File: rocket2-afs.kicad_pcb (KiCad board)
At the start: 4 copper layers, 70 x 50 mm, 72 parts, among them J1 ARMING_PLUG, J2 POWER, J3 E-MATCH_DROGUE, J4 SWD, J5 E-MATCH_RECOVERY, Q1 Q_NMOS_GSD, Q2 Q_NMOS_GSD, Q3 Q_NMOS_GSD, Q4 Q_NMOS_GSD, Q5 Q_NMOS_GSD, U2 LD1086DT33TR, U8 USBLC6-2SC6, Y1 16MHz

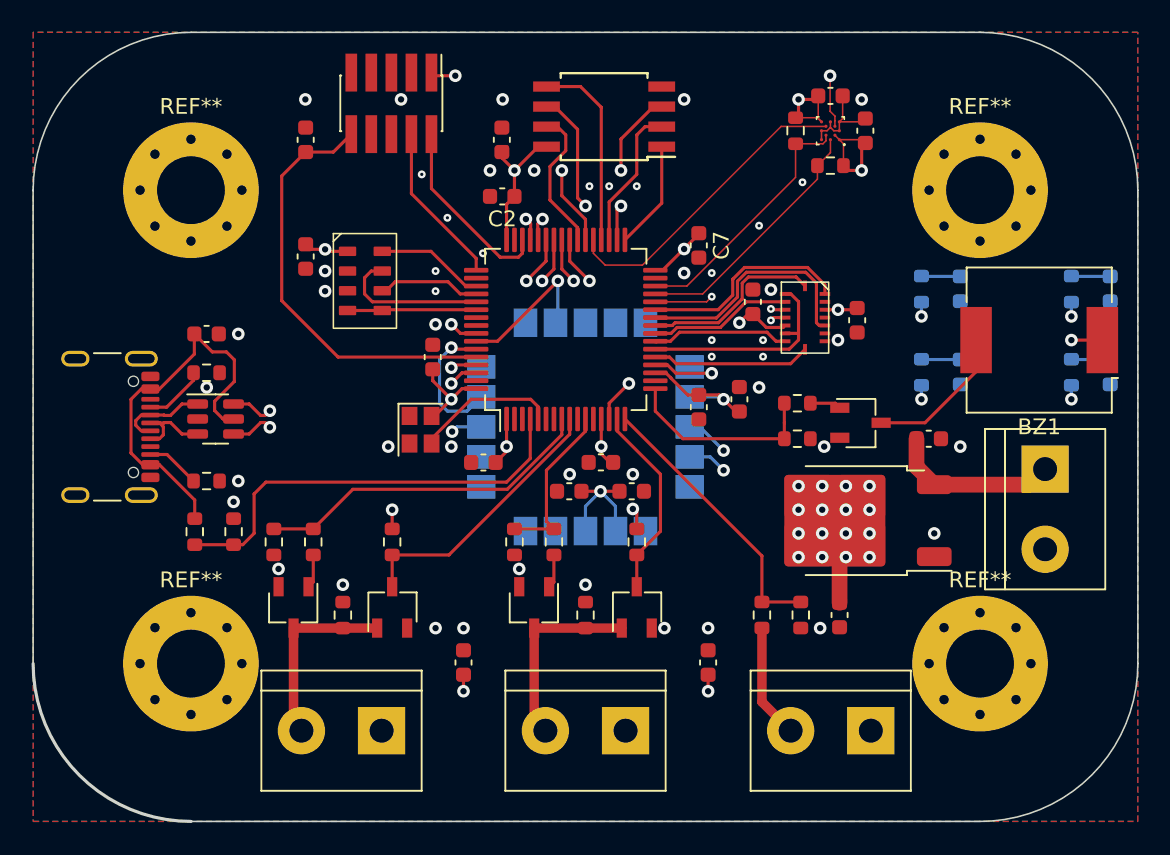
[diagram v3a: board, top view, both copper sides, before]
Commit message: Moved All Thick Components to "Front" Layer. Added Silkscreens
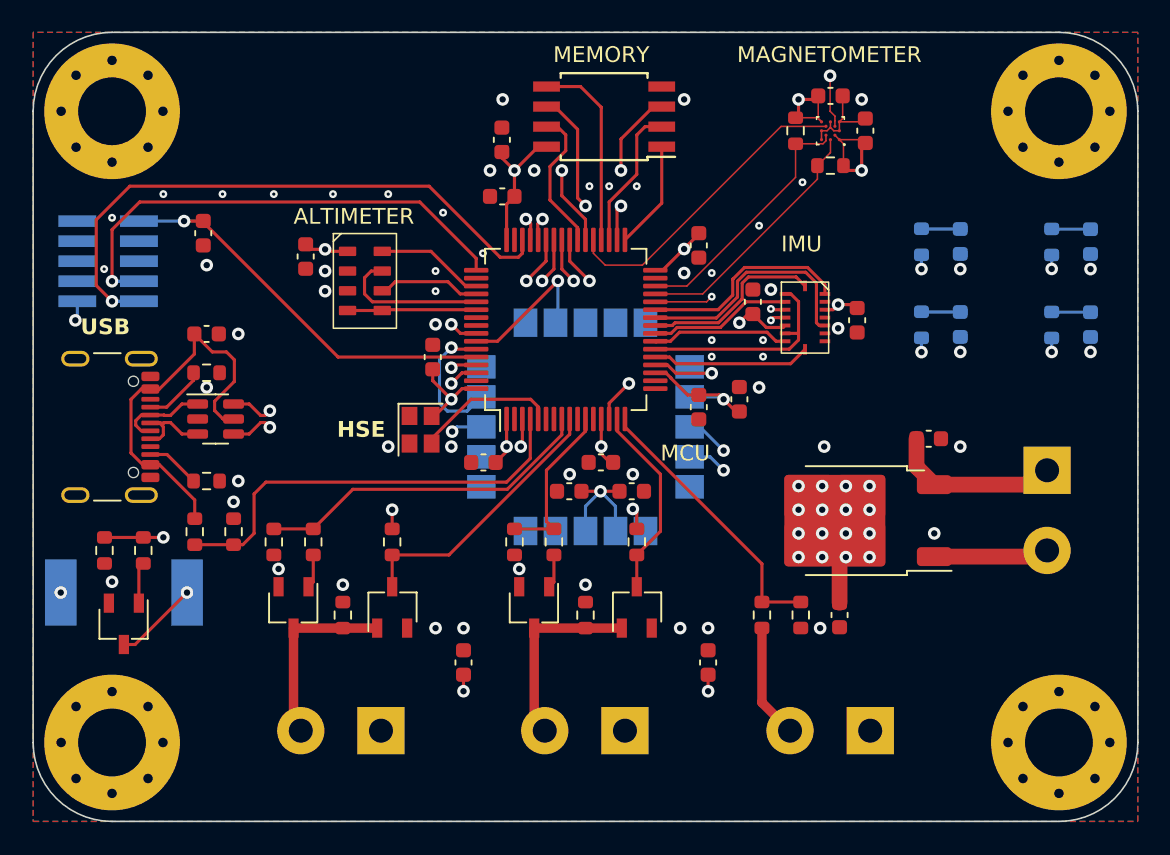
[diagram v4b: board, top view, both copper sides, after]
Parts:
- BZ1, J1, J2, J3, J4, J5: moved to B.Cu
- moved BZ1 60.2 mm to (125.8, 95.5), turned to 0 degrees
- moved Q5 48.4 mm to (125.8, 97.5), turned to -90 degrees
- moved R19 44.5 mm to (124.5, 92.8), turned to -90 degrees
- moved R20 42.5 mm to (127.0, 92.8), turned to -90 degrees
- moved J4 20.5 mm to (124.8, 74.5), turned to 0 degrees
- moved R9 11.7 mm to (184.5, 73.3)
- moved D3 11.7 mm to (187.0, 73.3)
- moved D2 9.77 mm to (178.8, 78.5)
- moved R7 9.77 mm to (176.3, 78.5)
- moved C1 8.78 mm to (130.8, 72.7), turned to 90 degrees
- moved REF** 7.07 mm to (125.0, 105.0)
- moved REF** 7.07 mm to (125.0, 65.0)
- moved REF** 7.07 mm to (185.0, 105.0)
- moved REF** 7.07 mm to (185.0, 65.0)
- moved D4 3.25 mm to (187.0, 78.5)
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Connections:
- U1 pad 17: BUZZER -> unconnected-(U1-PA3-Pad17)
- U1 pad 3: unconnected-(U1-PC14-Pad3) -> BUZZER
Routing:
- net DEBUG_SWDIO: track 12.0 -> 38.0 mm, vias 0 -> 1
- net DEBUCK_SWCLK: track 10.3 -> 31.0 mm, vias 0 -> 1
- net BUZZER: track 12.6 -> 30.6 mm, vias 0 -> 2
- net LED_STANDBY: track 34.6 -> 48.8 mm
- net LED_FLIGHT: track 44.6 -> 35.4 mm
- net GND: track 6.25 -> 13.6 mm, vias 49 -> 59
- net Net-(BZ1--): track 9.36 -> 5.36 mm, vias 0 -> 1
- net LED_ARMED: track 36.2 -> 39.2 mm
- net +3.3V: track 74.7 -> 72.6 mm
- net NRST: track 27.2 -> 26.2 mm, vias 0 -> 1
- net Net-(Q5-G): track 1.99 -> 2.63 mm
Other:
- outline, holes or cut-outs redrawn
- board text added: "(+)"
- board text added: "ALTIMETER"
- board text added: "ARMED"
- board text added: "ARMING PLUG"
- board text added: "BUZZER"
- board text added: "Caden Nguyen Robert Woo Eesh Vij Daniel He"
- board text added: "DEBUG"
- board text added: "DROGUE"
- board text added: "FLIGHT"
- board text added: "GPS"
- board text added: "HSE"
- board text added: "IMU"
- board text added: "MAGNETOMETER"
- board text added: "MAIN"
- board text added: "MCU"
- board text added: "MEMORY"
- board text added: "POWER"
- board text added: "STANDBY"
- board text added: "STORAGE"
- board text added: "UCI Rocket Project - Avionics Avionics Flight System Betelgeuse v2.1 03/12/2024"
- board text added: "USB"

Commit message: Silkscreen update.
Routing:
- net +3.3V: track 72.6 -> 73.2 mm
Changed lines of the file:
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@@
     )
     (stroke (width 0) (type solid)) (fill solid) (layer "B.SilkS"))
-  (gr_rect (start 160 65.25) (end 168.5 70.75)
+  (gr_rect (start 132.6875 62.25) (end 141.1875 67.75)
     (stroke (width 0.15) (type dash)) (fill none) (layer "B.SilkS"))
   (gr_poly
@@
     (effects (font (size 1 1) (thickness 0.1875) bold) (justify left bottom mirror))
   )
-  (gr_text "DEBUG" (at 134.25 69) (layer "B.SilkS")
+  (gr_text "DEBUG" (at 127.407441 79.75) (layer "B.SilkS")
     (effects (font (size 1 1) (thickness 0.1875) bold) (justify left bottom mirror))
   )
@@
     (effects (font (size 1 1) (thickness 0.1875) bold) (justify left bottom mirror))
   )
-  (gr_text "Caden Nguyen\nRobert Woo\nEesh Vij\nDaniel He" (at 164.25 70.25) (layer "B.SilkS")
+  (gr_text "Caden Nguyen\nRobert Woo\nEesh Vij\nDaniel He" (at 136.9375 67.30925) (layer "B.SilkS")
     (effects (font (size 0.75 0.75) (thickness 0.15)) (justify bottom mirror))
   )
@@
   (via (at 170 90.25) (size 0.8) (drill 0.4) (layers "F.Cu" "B.Cu") (net 3))
   (via (at 138.5 73.75) (size 0.8) (drill 0.4) (layers "F.Cu" "B.Cu") (net 3))
-  (via (at 122.675 78.25) (size 0.8) (drill 0.4) (layers "F.Cu" "B.Cu") (net 3))
+  (via (at 121.5 78.25) (size 0.8) (drill 0.4) (layers "F.Cu" "B.Cu") (net 3))
   (via (at 168.5 91.75) (size 0.8) (drill 0.4) (layers "F.Cu" "B.Cu") (net 3))
   (via (at 150.5 68.75) (size 0.8) (drill 0.4) (layers "F.Cu" "B.Cu") (net 3))
@@
   (segment (start 155.95 89.08) (end 156.9 90.03) (width 0.2) (layer "B.Cu") (net 3))
   (segment (start 163.75 83.25) (end 163.6 83.1) (width 0.2) (layer "B.Cu") (net 3))
-  (segment (start 122.8 77.04) (end 122.8 78.125) (width 0.2) (layer "B.Cu") (net 3))
-  (segment (start 122.8 78.125) (end 122.675 78.25) (width 0.2) (layer "B.Cu") (net 3))
+  (segment (start 121.59 78.25) (end 122.8 77.04) (width 0.2) (layer "B.Cu") (net 3))
   (segment (start 155.95 89.08) (end 155 90.03) (width 0.2) (layer "B.Cu") (net 3))
   (segment (start 163.6 83.1) (end 161.6 83.1) (width 0.2) (layer "B.Cu") (net 3))
+  (segment (start 121.5 78.25) (end 121.59 78.25) (width 0.2) (layer "B.Cu") (net 3))
   (segment (start 156.9 90.03) (end 156.9 91.6) (width 0.2) (layer "B.Cu") (net 3))
   (segment (start 166.18 97.745) (end 166.18 102.47) (width 0.6) (layer "F.Cu") (net 4))

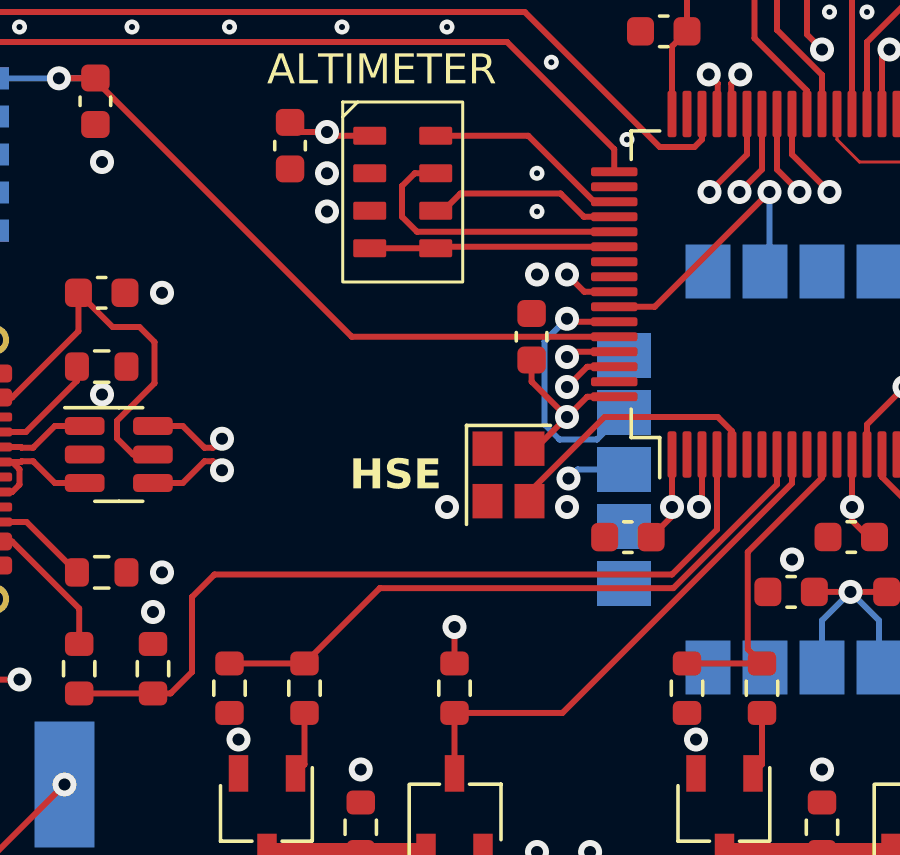
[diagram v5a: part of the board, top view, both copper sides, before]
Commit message: Adjusted VBUS
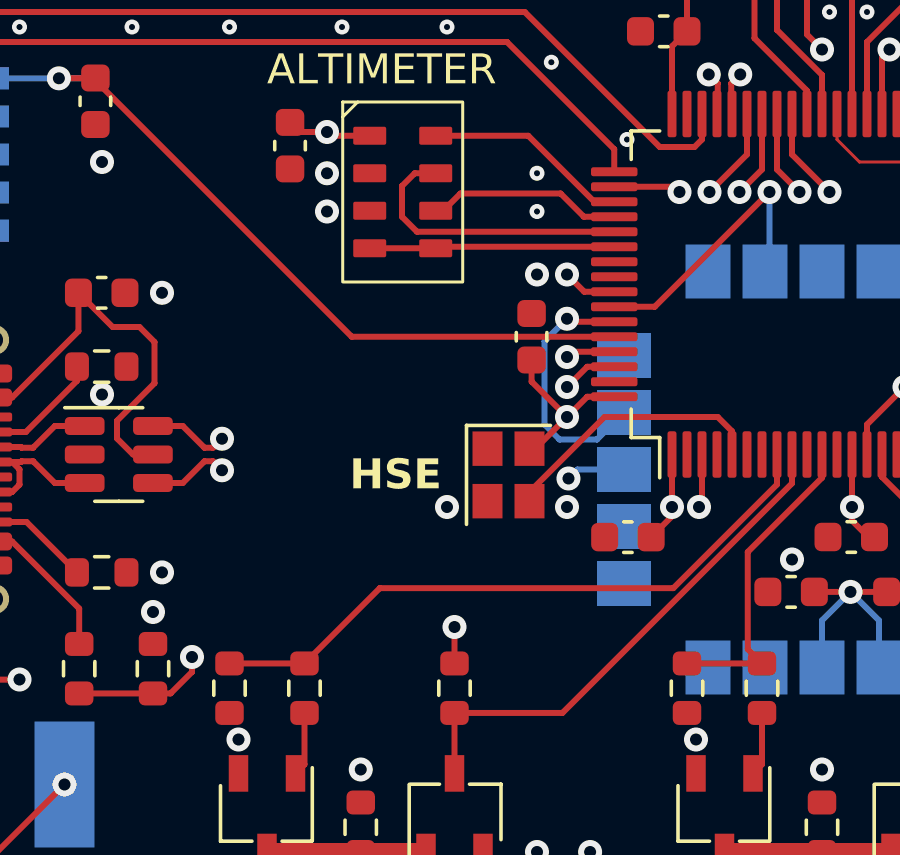
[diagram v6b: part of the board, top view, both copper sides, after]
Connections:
- U1 pad 4: VBUS_SENS -> unconnected-(U1-PC15-Pad4)
- U1 pad 42: LED_STANDBY -> VBUS_SENS
- U1 pad 43: LED_STORAGE -> LED_STANDBY
- U1 pad 50: unconnected-(U1-PA15-Pad50) -> LED_STORAGE
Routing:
- net VBUS_SENS: track 27.5 -> 40.0 mm, vias 0 -> 2
- net LED_STANDBY: track 48.8 -> 49.4 mm
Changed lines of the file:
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@@
   (net 41 "ALT_MOSI")
   (net 42 "ALT_CS")
-  (net 43 "unconnected-(U1-PA15-Pad50)")
+  (net 43 "unconnected-(U1-PC15-Pad4)")
   (net 44 "MAG_DRDY")
   (net 45 "MAG_INT")
@@
       (net 75 "BUZZER") (pinfunction "PC14") (pintype "bidirectional"))
     (pad "4" smd roundrect (at -5.675 -2.25 90) (size 1.55 0.3) (layers "F.Cu" "F.Paste" "F.Mask") (roundrect_rratio 0.25)
-      (net 77 "VBUS_SENS") (pinfunction "PC15") (pintype "bidirectional"))
+      (net 43 "unconnected-(U1-PC15-Pad4)") (pinfunction "PC15") (pintype "bidirectional+no_connect"))
     (pad "5" smd roundrect (at -5.675 -1.75 90) (size 1.55 0.3) (layers "F.Cu" "F.Paste" "F.Mask") (roundrect_rratio 0.25)
       (net 37 "HSE_IN") (pinfunction "PD0") (pintype "bidirectional"))
@@
       (net 30 "LED_FLIGHT") (pinfunction "PA8") (pintype "bidirectional"))
     (pad "42" smd roundrect (at 5.675 -0.75 90) (size 1.55 0.3) (layers "F.Cu" "F.Paste" "F.Mask") (roundrect_rratio 0.25)
-      (net 31 "LED_STANDBY") (pinfunction "PA9") (pintype "bidirectional"))
+      (net 77 "VBUS_SENS") (pinfunction "PA9") (pintype "bidirectional"))
     (pad "43" smd roundrect (at 5.675 -1.25 90) (size 1.55 0.3) (layers "F.Cu" "F.Paste" "F.Mask") (roundrect_rratio 0.25)
-      (net 32 "LED_STORAGE") (pinfunction "PA10") (pintype "bidirectional"))
+      (net 31 "LED_STANDBY") (pinfunction "PA10") (pintype "bidirectional"))
     (pad "44" smd roundrect (at 5.675 -1.75 90) (size 1.55 0.3) (layers "F.Cu" "F.Paste" "F.Mask") (roundrect_rratio 0.25)
       (net 70 "USB_D-") (pinfunction "PA11") (pintype "bidirectional"))
@@
       (net 12 "DEBUCK_SWCLK") (pinfunction "PA14") (pintype "bidirectional"))
     (pad "50" smd roundrect (at 3.25 -5.675 90) (size 0.3 1.55) (layers "F.Cu" "F.Paste" "F.Mask") (roundrect_rratio 0.25)
-      (net 43 "unconnected-(U1-PA15-Pad50)") (pinfunction "PA15") (pintype "bidirectional+no_connect"))
+      (net 32 "LED_STORAGE") (pinfunction "PA15") (pintype "bidirectional"))
     (pad "51" smd roundrect (at 2.75 -5.675 90) (size 0.3 1.55) (layers "F.Cu" "F.Paste" "F.Mask") (roundrect_rratio 0.25)
       (net 39 "ALT_SCK") (pinfunction "PC10") (pintype "bidirectional"))
@@
   (segment (start 154.25 75.75) (end 154.25 80.75) (width 0.2) (layer "In1.Cu") (net 30))
   (segment (start 176.29 79.365) (end 176.29 80.25) (width 0.2) (layer "B.Cu") (net 30))
-  (segment (start 153 75) (end 153 73.15) (width 0.2) (layer "F.Cu") (net 31))
-  (segment (start 152.25 75.75) (end 153 75) (width 0.2) (layer "F.Cu") (net 31))
+  (segment (start 152.5 74.5) (end 152.5 73.15) (width 0.2) (layer "F.Cu") (net 31))
+  (segment (start 151.25 75.75) (end 152.5 74.5) (width 0.2) (layer "F.Cu") (net 31))
   (via (at 184.54 74.99) (size 0.8) (drill 0.4) (layers "F.Cu" "B.Cu") (net 31))
-  (via (at 152.25 75.75) (size 0.8) (drill 0.4) (layers "F.Cu" "B.Cu") (net 31))
-  (segment (start 182.875 81) (end 178.5 81) (width 0.2) (layer "In1.Cu") (net 31))
+  (via (at 151.25 75.75) (size 0.8) (drill 0.4) (layers "F.Cu" "B.Cu") (net 31))
+  (segment (start 183.5 80.375) (end 182.875 81) (width 0.2) (layer "In1.Cu") (net 31))
   (segment (start 184.54 74.99) (end 183.5 76.03) (width 0.2) (layer "In1.Cu") (net 31))
+  (segment (start 151.25 78.5) (end 151.25 75.75) (width 0.2) (layer "In1.Cu") (net 31))
+  (segment (start 157.75 85) (end 151.25 78.5) (width 0.2) (layer "In1.Cu") (net 31))
+  (segment (start 182.875 81) (end 178.5 81) (width 0.2) (layer "In1.Cu") (net 31))
   (segment (start 183.5 76.03) (end 183.5 80.375) (width 0.2) (layer "In1.Cu") (net 31))
-  (segment (start 183.5 80.375) (end 182.875 81) (width 0.2) (layer "In1.Cu") (net 31))
   (segment (start 174.5 85) (end 157.75 85) (width 0.2) (layer "In1.Cu") (net 31))
   (segment (start 178.5 81) (end 174.5 85) (width 0.2) (layer "In1.Cu") (net 31))
-  (segment (start 157.75 85) (end 152.25 79.5) (width 0.2) (layer "In1.Cu") (net 31))
-  (segment (start 152.25 79.5) (end 152.25 75.75) (width 0.2) (layer "In1.Cu") (net 31))
   (segment (start 184.54 74.105) (end 184.54 74.99) (width 0.2) (layer "B.Cu") (net 31))
-  (segment (start 152.5 74.5) (end 152.5 73.15) (width 0.2) (layer "F.Cu") (net 32))
-  (segment (start 151.25 75.75) (end 152.5 74.5) (width 0.2) (layer "F.Cu") (net 32))
-  (via (at 151.25 75.75) (size 0.8) (drill 0.4) (layers "F.Cu" "B.Cu") (net 32))
+  (segment (start 150.075 75.575) (end 150.25 75.75) (width 0.2) (layer "F.Cu") (net 32))
+  (segment (start 148.075 75.575) (end 150.075 75.575) (width 0.2) (layer "F.Cu") (net 32))
+  (via (at 150.25 75.75) (size 0.8) (drill 0.4) (layers "F.Cu" "B.Cu") (net 32))
   (via (at 184.54 80.25) (size 0.8) (drill 0.4) (layers "F.Cu" "B.Cu") (free) (net 32))
-  (segment (start 151.25 79.25) (end 157.5 85.5) (width 0.2) (layer "In1.Cu") (net 32))
-  (segment (start 184.54 80.25) (end 183.29 81.5) (width 0.2) (layer "In1.Cu") (net 32))
-  (segment (start 157.5 85.5) (end 174.75 85.5) (width 0.2) (layer "In1.Cu") (net 32))
-  (segment (start 178.75 81.5) (end 182.5 81.5) (width 0.2) (layer "In1.Cu") (net 32))
-  (segment (start 183.29 81.5) (end 182.5 81.5) (width 0.2) (layer "In1.Cu") (net 32))
-  (segment (start 151.25 75.75) (end 151.25 79.25) (width 0.2) (layer "In1.Cu") (net 32))
+  (segment (start 150.25 78.25) (end 157.5 85.5) (width 0.2) (layer "In1.Cu") (net 32))
+  (segment (start 178.75 81.5) (end 183.29 81.5) (width 0.2) (layer "In1.Cu") (net 32))
   (segment (start 174.75 85.5) (end 178.75 81.5) (width 0.2) (layer "In1.Cu") (net 32))
+  (segment (start 157.5 85.5) (end 174.75 85.5) (width 0.2) (layer "In1.Cu") (net 32))
+  (segment (start 150.25 75.75) (end 150.25 78.25) (width 0.2) (layer "In1.Cu") (net 32))
+  (segment (start 183.29 81.5) (end 184.54 80.25) (width 0.2) (layer "In1.Cu") (net 32))
   (segment (start 184.54 79.365) (end 184.54 80.25) (width 0.2) (layer "B.Cu") (net 32))
   (segment (start 153.25 75.75) (end 149.425 79.575) (width 0.2) (layer "F.Cu") (net 33))
@@
   (segment (start 145.2 92) (end 128.25 92) (width 0.2) (layer "In1.Cu") (net 75))
   (segment (start 150.9 86.25) (end 150.9 86.3) (width 0.2) (layer "In1.Cu") (net 75))
-  (segment (start 151.5 87) (end 151.5 84.5) (width 0.2) (layer "F.Cu") (net 77))
   (segment (start 132.7 92.465) (end 130.24 92.465) (width 0.2) (layer "F.Cu") (net 77))
-  (segment (start 134 91.75) (end 134 89.25) (width 0.2) (layer "F.Cu") (net 77))
-  (segment (start 134 89.25) (end 134.75 88.5) (width 0.2) (layer "F.Cu") (net 77))
-  (segment (start 134.75 88.5) (end 150 88.5) (width 0.2) (layer "F.Cu") (net 77))
+  (segment (start 134 91.75) (end 134 91.25) (width 0.2) (layer "F.Cu") (net 77))
+  (segment (start 153 75) (end 153 73.15) (width 0.2) (layer "F.Cu") (net 77))
+  (segment (start 152.25 75.75) (end 153 75) (width 0.2) (layer "F.Cu") (net 77))
   (segment (start 132.7 92.465) (end 133.285 92.465) (width 0.2) (layer "F.Cu") (net 77))
-  (segment (start 150 88.5) (end 151.5 87) (width 0.2) (layer "F.Cu") (net 77))
   (segment (start 133.285 92.465) (end 134 91.75) (width 0.2) (layer "F.Cu") (net 77))
+  (via (at 152.25 75.75) (size 0.8) (drill 0.4) (layers "F.Cu" "B.Cu") (net 77))
+  (via (at 134 91.25) (size 0.8) (drill 0.4) (layers "F.Cu" "B.Cu") (net 77))
+  (segment (start 134 91.25) (end 143.5 91.25) (width 0.2) (layer "In1.Cu") (net 77))
+  (segment (start 144.5 90.25) (end 144.5 78.25) (width 0.2) (layer "In1.Cu") (net 77))
+  (segment (start 144.5 78.25) (end 148 74.75) (width 0.2) (layer "In1.Cu") (net 77))
+  (segment (start 143.5 91.25) (end 144.5 90.25) (width 0.2) (layer "In1.Cu") (net 77))
+  (segment (start 151.25 74.75) (end 152.25 75.75) (width 0.2) (layer "In1.Cu") (net 77))
+  (segment (start 148 74.75) (end 151.25 74.75) (width 0.2) (layer "In1.Cu") (net 77))
   (zone (net 1) (net_name "GND") (layers "F&B.Cu") (name "Control1") (hatch edge 0.5)
     (priority 3)
